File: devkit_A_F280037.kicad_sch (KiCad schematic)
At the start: 4 parts, among them J1 DEVKIT_C2000_ROW_A, J2 DEVKIT_C2000_ROW_B, J3 JTAG_CTBP_10, U1 TMS320F280037CSPM

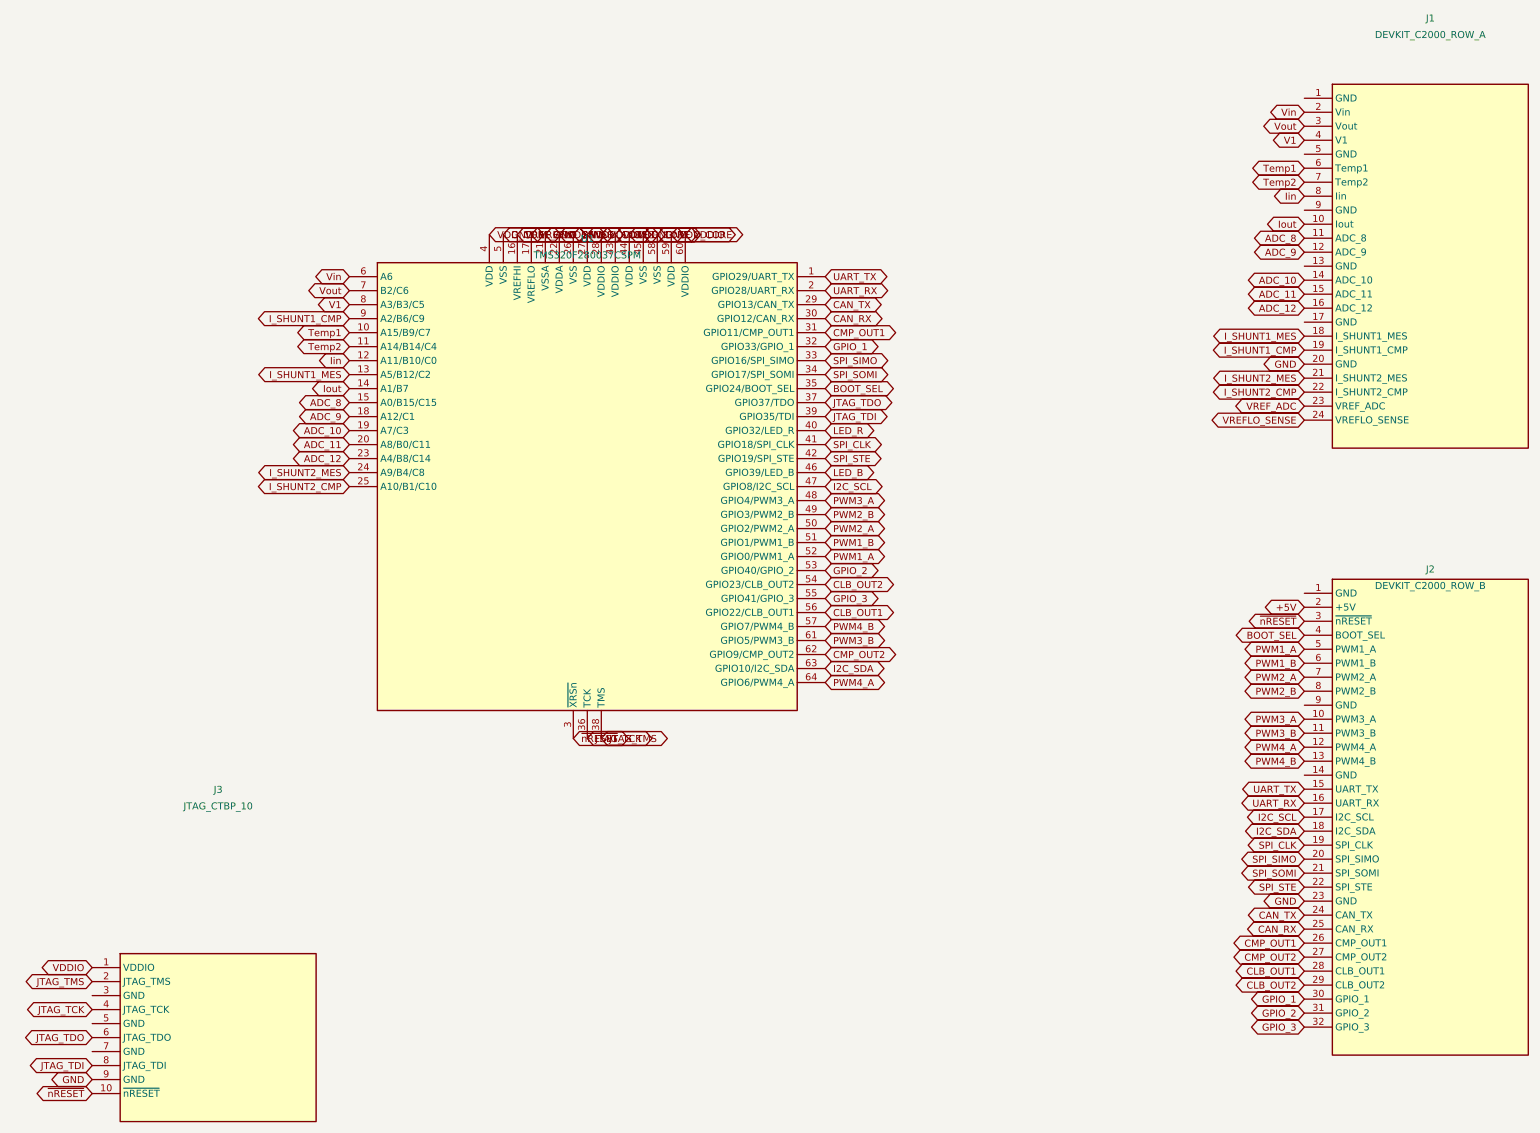
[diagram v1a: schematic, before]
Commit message: Devkit en 2 x 28 et ESP32-C6-DevKitC-1 monte sur le shield (J9, J10)
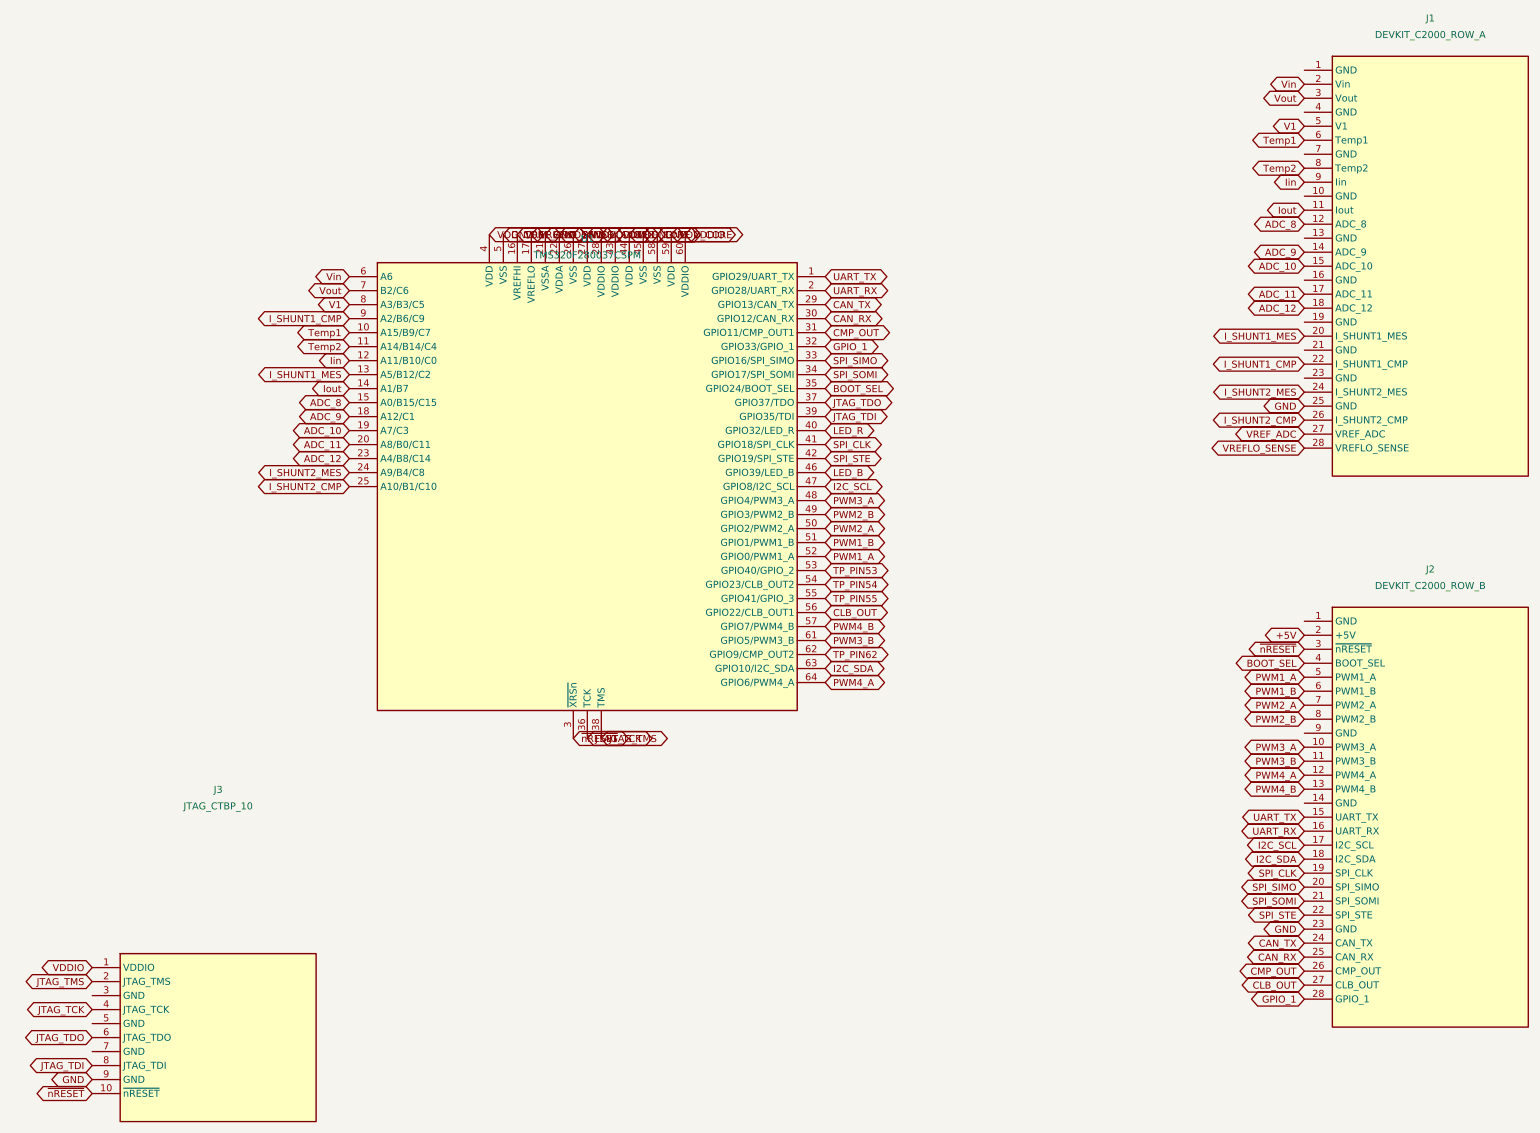
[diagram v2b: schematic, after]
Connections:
- net ADC_10: now also J1.15 (ADC_10); no longer J1.14 (ADC_10)
- net ADC_11: now also J1.17 (ADC_11); no longer J1.15 (ADC_11)
- net ADC_12: now also J1.18 (ADC_12); no longer J1.16 (ADC_12)
- net ADC_8: now also J1.12 (ADC_8); no longer J1.11 (ADC_8)
- net ADC_9: now also J1.14 (ADC_9); no longer J1.12 (ADC_9)
- net GND: now also J1.25 (GND); no longer J1.20 (GND)
- net GPIO_1: now also J2.28 (GPIO_1); no longer J2.30 (GPIO_1)
- net I_SHUNT1_CMP: now also J1.22 (I_SHUNT1_CMP); no longer J1.19 (I_SHUNT1_CMP)
- net I_SHUNT1_MES: now also J1.20 (I_SHUNT1_MES); no longer J1.18 (I_SHUNT1_MES)
- net I_SHUNT2_CMP: now also J1.26 (I_SHUNT2_CMP); no longer J1.22 (I_SHUNT2_CMP)
- net I_SHUNT2_MES: now also J1.24 (I_SHUNT2_MES); no longer J1.21 (I_SHUNT2_MES)
- net Iin: now also J1.9 (Iin); no longer J1.8 (Iin)
- net Iout: now also J1.11 (Iout); no longer J1.10 (Iout)
- net Temp2: now also J1.8 (Temp2); no longer J1.7 (Temp2)
- net V1: now also J1.5 (V1); no longer J1.4 (V1)
- net VREFLO_SENSE: now also J1.28 (VREFLO_SENSE); no longer J1.24 (VREFLO_SENSE)
- net VREF_ADC: now also J1.27 (VREF_ADC); no longer J1.23 (VREF_ADC)
- net CLB_OUT1 renamed CLB_OUT
- net CLB_OUT: now also J2.27 (CLB_OUT); no longer J2.28 (CLB_OUT1)
- net CLB_OUT2 renamed TP_PIN54
- net TP_PIN54: no longer J2.29 (CLB_OUT2)
- net CMP_OUT1 renamed CMP_OUT
- net CMP_OUT2 renamed TP_PIN62
- net TP_PIN62: no longer J2.27 (CMP_OUT2)
- net GPIO_2 renamed TP_PIN53
- net TP_PIN53: no longer J2.31 (GPIO_2)
- net GPIO_3 renamed TP_PIN55
- net TP_PIN55: no longer J2.32 (GPIO_3)

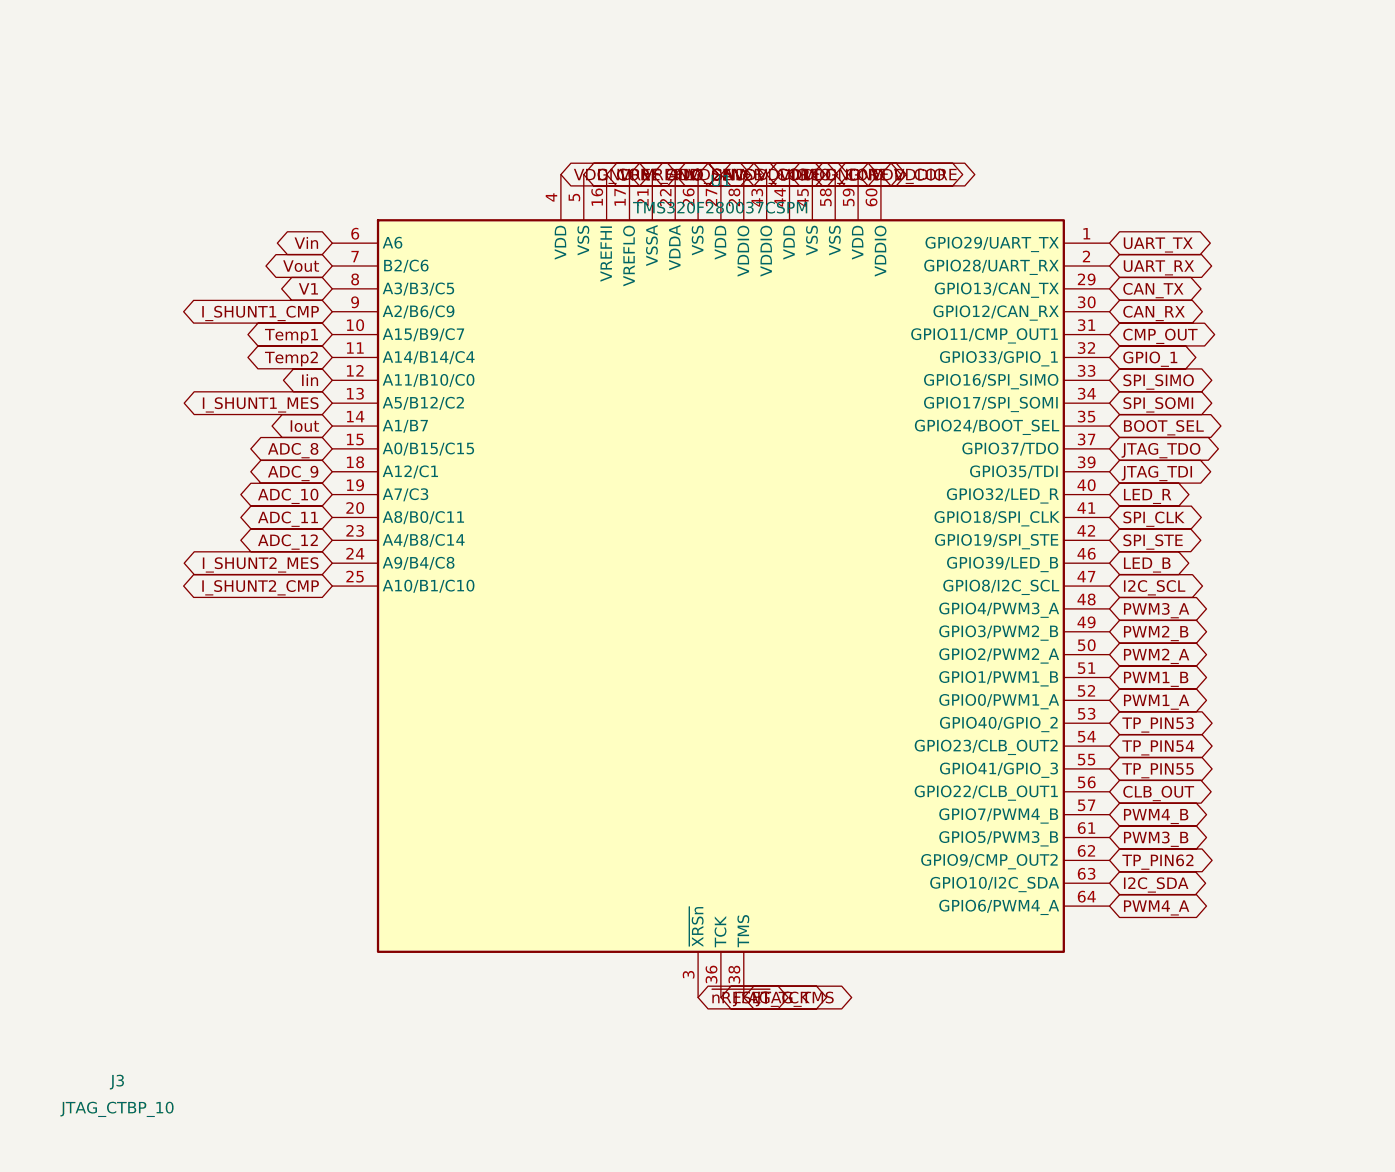
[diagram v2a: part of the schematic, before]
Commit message: Symboles MCU en carre LQFP-64, 16 broches par cote de 1 a 64
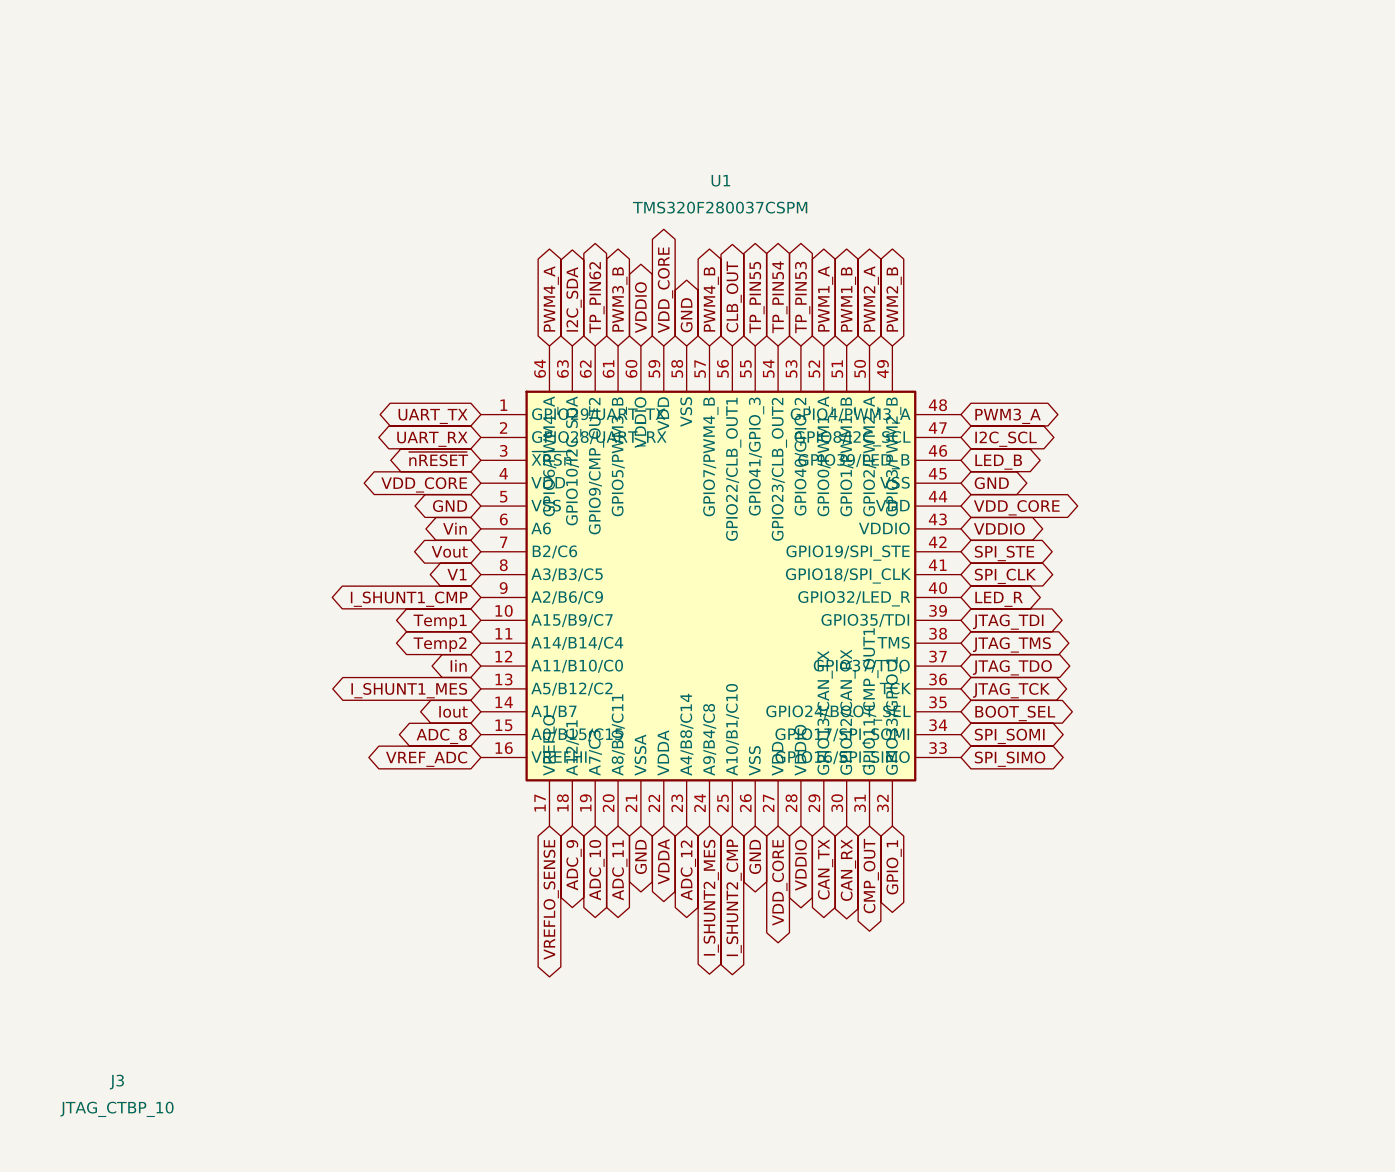
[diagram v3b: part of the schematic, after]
